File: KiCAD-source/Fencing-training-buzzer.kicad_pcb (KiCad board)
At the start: 2 copper layers, 26 x 62.2 mm, 13 parts, among them J1 Con, J2 DC Jack 5V, U1 74HC02

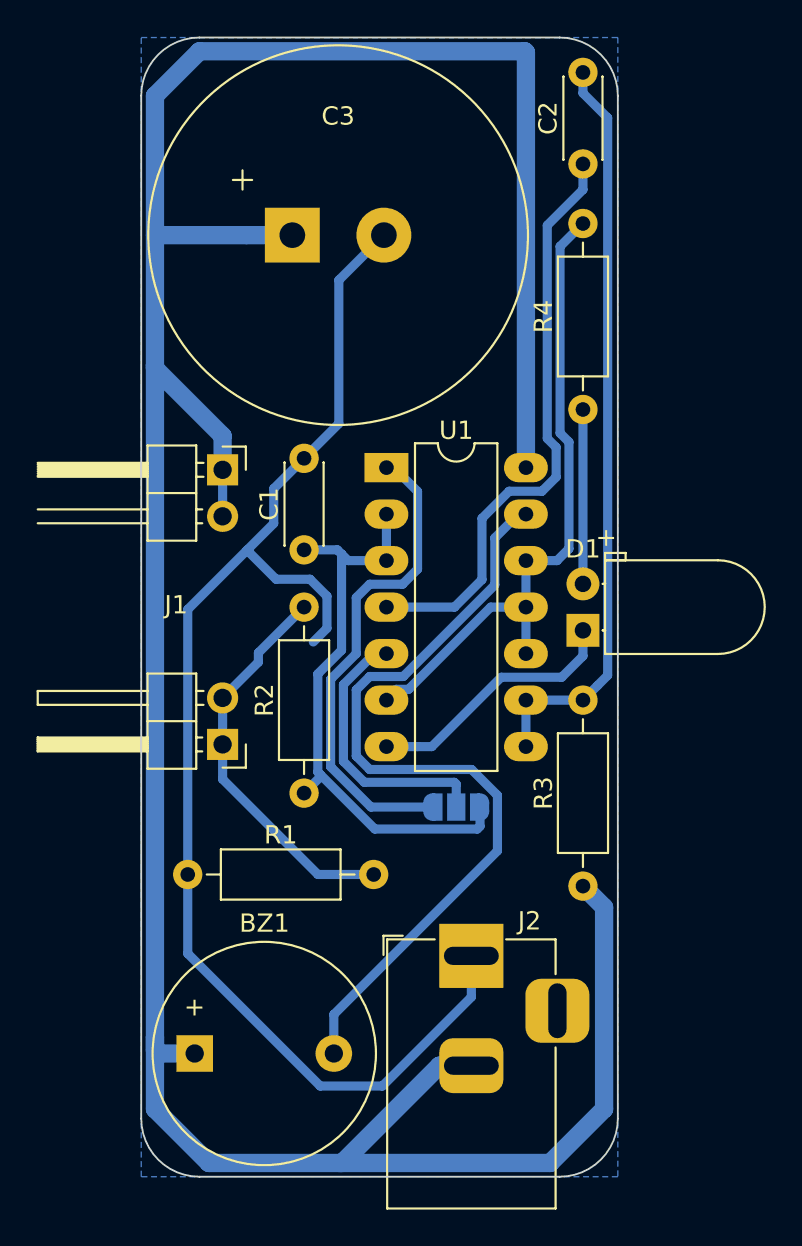
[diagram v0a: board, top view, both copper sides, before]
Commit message: Fix reverse polarity error at the barrel jack
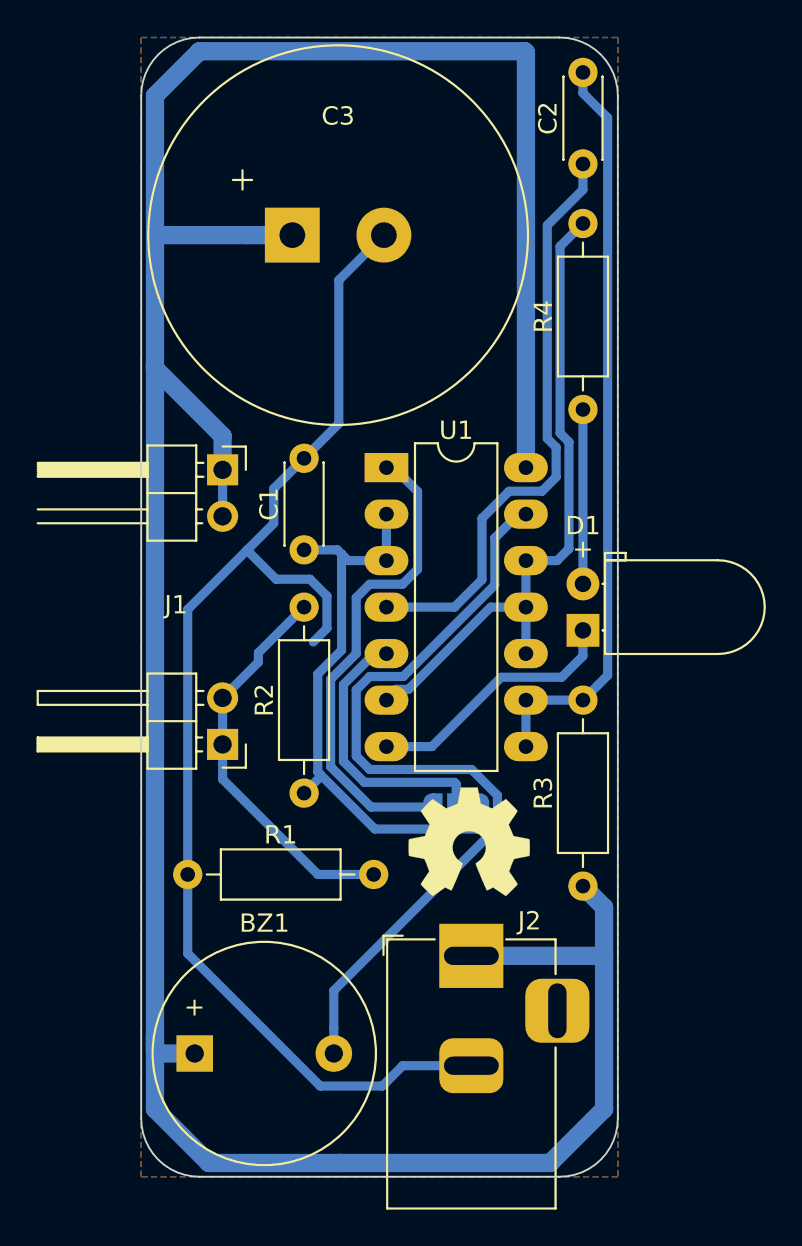
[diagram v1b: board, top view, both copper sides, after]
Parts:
- added REF**: OSHW-Symbol_6.7x6mm_SilkScreen, Symbol:OSHW-Symbol_6.7x6mm_SilkScreen, B.Cu at (158.8, 73.7)
- added REF**: OSHW-Symbol_6.7x6mm_SilkScreen, Symbol:OSHW-Symbol_6.7x6mm_SilkScreen, F.Cu at (159.5, 101.7)
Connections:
- J2 pad 1: GND -> VCC
- J2 pad 2: VCC -> GND
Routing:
- net GND: track 88.8 -> 85.0 mm
- net VCC: track 168.7 -> 166.7 mm
- added copper zone on F.Cu, net GND
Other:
- board text added: "epee"
- board text added: "foil"
- board text added: "github.com/julianschuler/fencing-training-buzzer"
- board text added: "open source hardware"
- board text removed: "Epee"
- board text removed: "Foil"
